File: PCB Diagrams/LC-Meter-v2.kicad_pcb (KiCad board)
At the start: 2 copper layers, 88.9 x 100.3 mm, 32 parts, among them J1 Power, J2 External, J3 Cx/Lx, J4 GND, J5 Display I2C, J6 Base 01, J7 Top 01, J8 Base 02, J9 Top 02, SW1 Select, SW2 High, SW3 Med, SW4 Low, U1 LM358

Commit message: first commit
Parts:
- added J10: Ext/A, Connector_PinHeader_2.54mm:PinHeader_1x01_P2.54mm_Horizontal, F.Cu at (88.9, 134.6)
- added J11: Ext/B, Connector_PinHeader_2.54mm:PinHeader_1x01_P2.54mm_Horizontal, F.Cu at (142.2, 76.2)
- J6: value Base 01 -> CxMode/A
- J7: value Top 01 -> CxMode/B
- J8: value Base 02 -> Select/A
- J9: value Top 02 -> Select/B
- moved J2 18.3 mm to (142.2, 71.1)
- moved J5 5.08 mm to (88.9, 114.3)
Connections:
- A1 pad 23: unconnected-(A1-A4-Pad23) -> Net-(A1-A4)
- A1 pad 25: Net-(A1-A6) -> unconnected-(A1-A6-Pad25)
- A1 pad 26: Net-(A1-A7) -> unconnected-(A1-A7-Pad26)
- C1 pad 1: Net-(J2-Pin_2) -> Net-(J8-Pin_1)
- J2 pad 1: Net-(A1-A0) -> Net-(J11-Pin_1)
- J2 pad 2: Net-(J2-Pin_2) -> GND
- J5 pad 2: Net-(A1-A6) -> Net-(A1-A4)
- J5 pad 3: Net-(A1-A7) -> Net-(A1-A5)
- J8 pad 1: Net-(J2-Pin_2) -> Net-(J8-Pin_1)
- R5 pad 1: Net-(J2-Pin_2) -> Net-(J8-Pin_1)
- U1 pad 3: Net-(J2-Pin_2) -> Net-(J8-Pin_1)
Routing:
- net Net-(J2-Pin_2): track 77.1 -> 0.00 mm
- net Net-(J8-Pin_1): track 0.00 -> 65.8 mm
- net GND: track 157.9 -> 177.8 mm
- net Net-(J10-Pin_1): track 39.5 -> 47.7 mm
- net Net-(A1-A0): track 116.8 -> 109.1 mm
- net Net-(J11-Pin_1): track 0.00 -> 5.08 mm
- net Net-(A1-A7): track 5.08 -> 0.00 mm
- net Net-(A1-A6): track 5.08 -> 0.00 mm
- net Net-(A1-A5): track 0.00 -> 5.07 mm
- net Net-(A1-A4): track 0.00 -> 5.07 mm
- net +5V: track 119.3 -> 121.8 mm

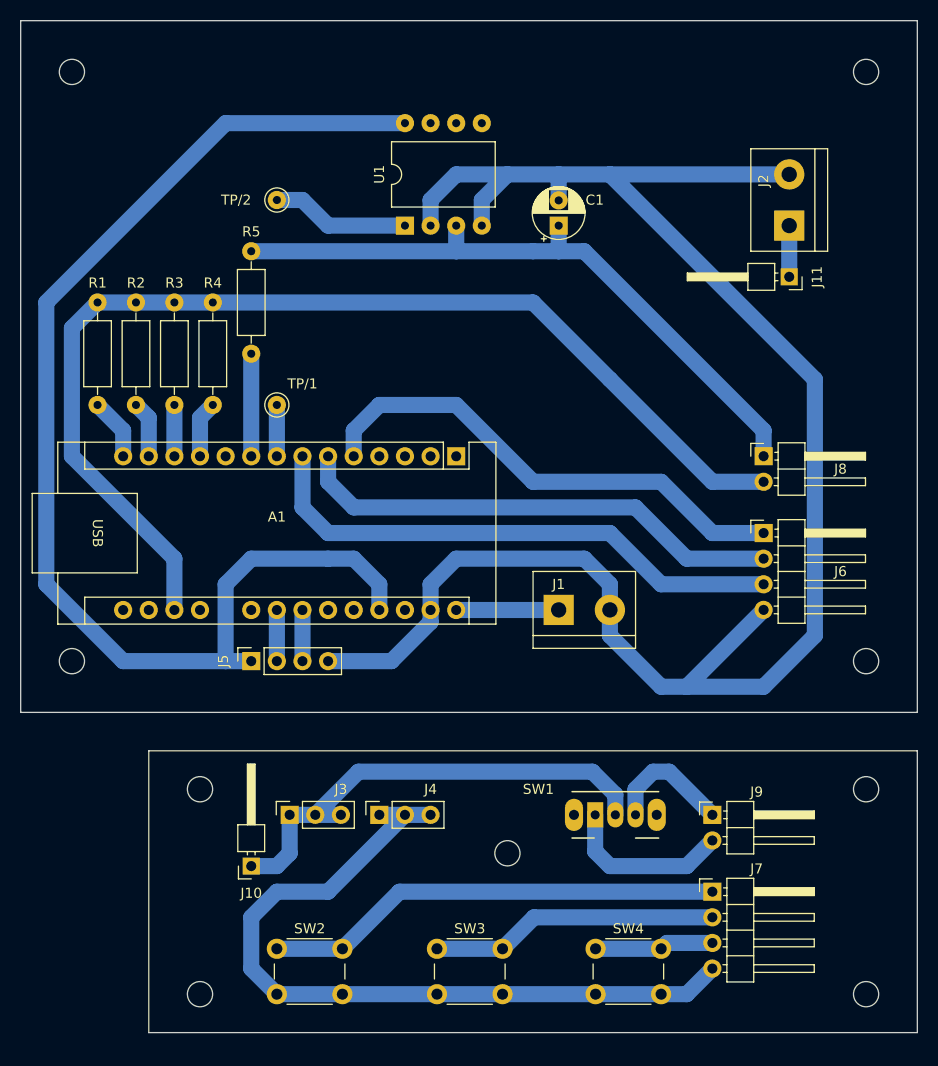
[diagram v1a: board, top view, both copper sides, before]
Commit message: pin position & component annotations improvements
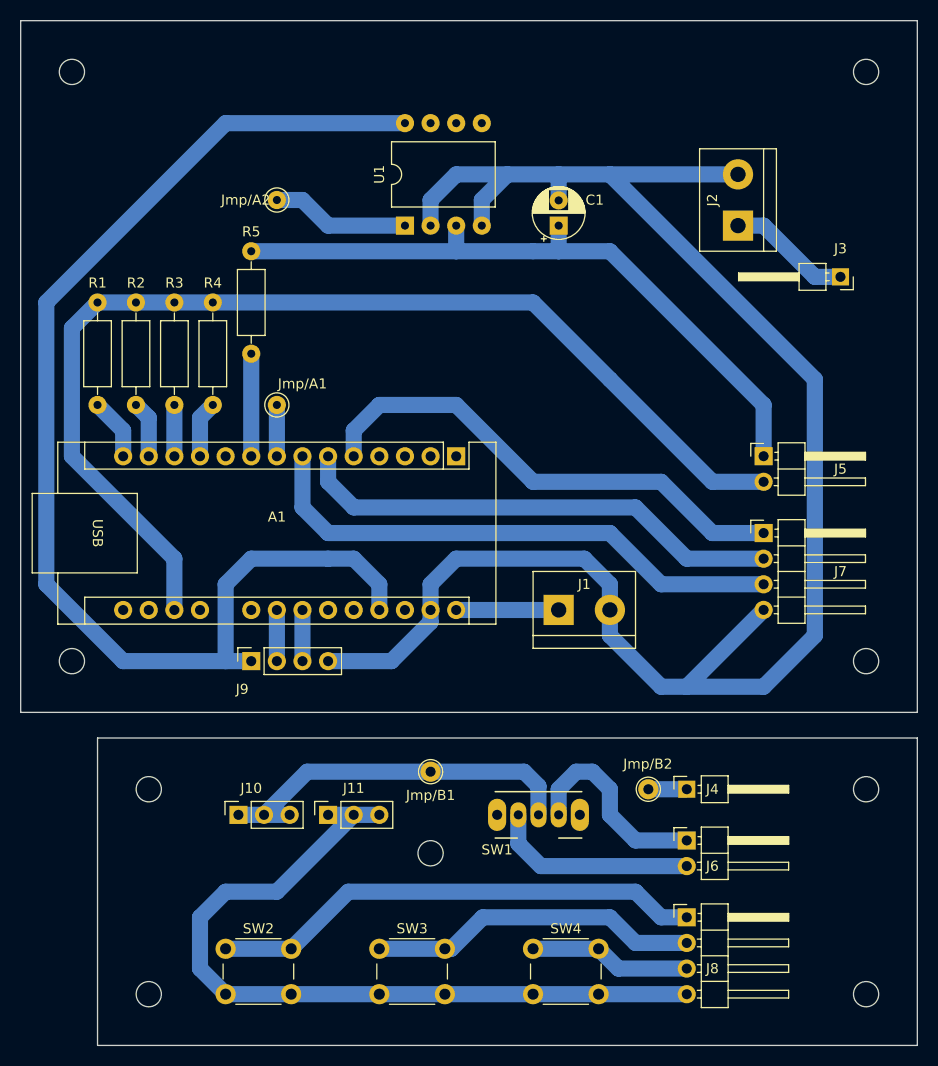
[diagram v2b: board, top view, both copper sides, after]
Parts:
- added Jmp/B1: Bridge, TestPoint:TestPoint_THTPad_D2.0mm_Drill1.0mm, F.Cu at (106.7, 125.3)
- added Jmp/B2: Bridge, TestPoint:TestPoint_THTPad_D2.0mm_Drill1.0mm, F.Cu at (128.3, 127.0)
- J3: renamed from J11; value Ext/B -> Ext/A
- J4: renamed from J10; value Ext/A -> Ext/B
- moved J4 43.8 mm to (132.1, 127.0), turned to 0 degrees
- moved SW1 7.62 mm to (115.4, 129.5)
- moved H9 7.62 mm to (106.7, 133.3)
- moved SW4 6.20 mm to (116.8, 142.8)
- moved SW3 5.72 mm to (101.6, 142.8)
- moved J2 5.08 mm to (137.2, 71.1)
- moved H5 5.08 mm to (78.7, 127.0)
- moved H8 5.08 mm to (78.7, 147.3)
- moved J10 5.08 mm to (87.6, 129.5)
- moved J11 5.08 mm to (96.5, 129.5)
- moved SW2 5.08 mm to (86.4, 142.8)
- moved J3 5.08 mm to (147.3, 76.2)
- moved J6 3.59 mm to (132.1, 132.1)
- moved J8 3.59 mm to (132.1, 139.7)
- renumbered J3 to J10, J4 to J11, J8 to J5, J9 to J6, J6 to J7, J7 to J8, J5 to J9, TP/1 to Jmp/A1, TP/2 to Jmp/A2
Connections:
- J4 pad 1: Net-(J10-Pin_1) -> Net-(J4-Pin_1)
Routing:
- net Net-(J10-Pin_1): track 47.7 -> 37.5 mm
- net Net-(J6-Pin_1): track 12.7 -> 20.3 mm
- net Net-(J2-Pin_1): track 5.08 -> 12.3 mm
- net GND: track 177.8 -> 172.7 mm
- net Net-(J8-Pin_3): track 11.8 -> 16.1 mm
- net Net-(J4-Pin_1): track 0.00 -> 3.81 mm
- net Net-(J8-Pin_2): track 28.6 -> 32.2 mm
- net Net-(J8-Pin_1): track 45.5 -> 49.1 mm
- net Net-(J6-Pin_2): track 16.9 -> 20.5 mm
- net Net-(J11-Pin_1): track 77.4 -> 78.9 mm
- net Net-(J5-Pin_1): track 65.8 -> 67.3 mm
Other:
- board size 88.9 x 100.3 mm -> 88.9 x 101.6 mm
